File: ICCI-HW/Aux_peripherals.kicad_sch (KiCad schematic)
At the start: 35 parts

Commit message: usb PD started
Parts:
- added C? (x4): 100n, symbol Device:C
- added C? (x3): 4.7u, symbol Device:C
- added D?: Bat60B, symbol Device:D_Schottky
- added FB? (x2): BLM15HD102SN1D, symbol Device:FerriteBead_Small
- added NT?: NetTie_2, symbol Device:NetTie_2
- added R? (x3): R, symbol Device:R
- BT?: value Battery_Cell -> 2032 Cell
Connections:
- net VBATT is gone; now on net VBAT: R?.2, U?.3 (V_BCKP)
- net +3V3: now also U?.20 (VDD), C?.1, C?.1, C?.1, C?.1, R?.1, R?.1, R?.1
- net GND: now also U?.2 (MOSI), U?.8 (VSS), C?.2, C?.2, C?.2, C?.2, C?.2, C?.2, C?.2
- net RXD: now also FB?.1
- net TXD: now also FB?.1
- net SCL: now reaches U?.1 (SCL)
- net PFI: now reaches U?.14 (~{PFO})
- net ~{PFO}: now reaches U?.15 (PFI)
- net ~{PFO}: now also R?.2
- net ~{RTS}: now reaches U?.16 (~{RTS})
- net ~{RTS}: now also R?.2
- net ~{INT}: now reaches U?.17 (~{INT})
- net BBS: now reaches U?.18 (BBS)
- net BBS: now also NT?.2
- net VBAT: now reaches U?.19 (VBAT)
- net VBAT: now also C?.1, C?.1, C?.1, D?.1 (K)
- net SDA: now reaches U?.4 (SDA/~{CE})
- net IFS: now reaches U?.5 (IFS)
- net IFS: now also NT?.1
- net ~{TS}: now reaches U?.6 (~{TS})
- net CLKOUT: now reaches U?.7 (CLKOUT)
- net CLKOUT: now also R?.2
- net at BT?.1 (+): now also D?.2 (A)
- net EXTINT renamed GPS_EXTINT
- net TP renamed GPS_TP
- net ~{RESET} renamed ~{GPS_RESET}
- new net GPS_RXD: FB?.2
- new net GPS_TXD: FB?.2
- no-connect marks 2 -> 3
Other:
- note added: "BATT on GPS for hot start"
- note added: "BATT on RTC for time"
- note added: "FORK RTC/GPS GITHUB"
- note added: "VCC decoup"
- note added: "Vbat decoup"
- note removed: "Possibilità di non montarlo"
- moved on the sheet: BT?, Q?, R?, U?

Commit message: updated
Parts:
- removed C? (x4): 100n, symbol Device:C
- removed R? (x4): 10k, symbol Device:R
- removed SW?: SW_BOOT, symbol Switch:SW_Push
- removed SW?: SW_LOG_SD, symbol Switch:SW_Push
- removed SW?: SW_RST_PROV, symbol Switch:SW_Push
- removed SW?: SW_RST, symbol Switch:SW_Push
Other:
- note removed: "BUTTONS"

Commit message: updated
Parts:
- removed FB? (x2): BLM15HD102SN1D, symbol Device:FerriteBead_Small
- added R? (x2): 4.7k, symbol Device:R
- R?: Place (none) -> DNP; now left out of the parts list
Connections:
- net SCL is gone; now on net SCL1: U?.1 (SCL)
- net SDA is gone; now on net SDA1: U?.4 (SDA/~{CE})
- net +3V3: now also R?.1, R?.1
- net SCL1: now reaches U?.12 (SCL)
- net SCL1: now also R?.2
- net SDA1: now reaches U?.9 (SDA)
- net SDA1: now also R?.2
- net CLKOUT renamed RTC_CLKOUT
- net RXD: no longer names the net of U?.14 (RXD)
- net SD_CLK renamed VSPI_CLK
- net SD_MISO renamed VSPI_MISO
- net SD_MOSI renamed VSPI_MOSI
- net TXD: no longer names the net of U?.13 (TXD)
- net ~{PFO} renamed ~{RTC_PFO}
- net ~{RTS} renamed ~{RTC_RTS}
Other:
- note added: "BATT on GPS for hot start, RTC time can't be read BATT on RTC for time"
- note added: "DA CONTROLLARE TUUTA STA ROBA"
- note removed: "BATT on GPS for hot start"
- note removed: "BATT on RTC for time"
- moved on the sheet: BZ?, D?, Q?, R?

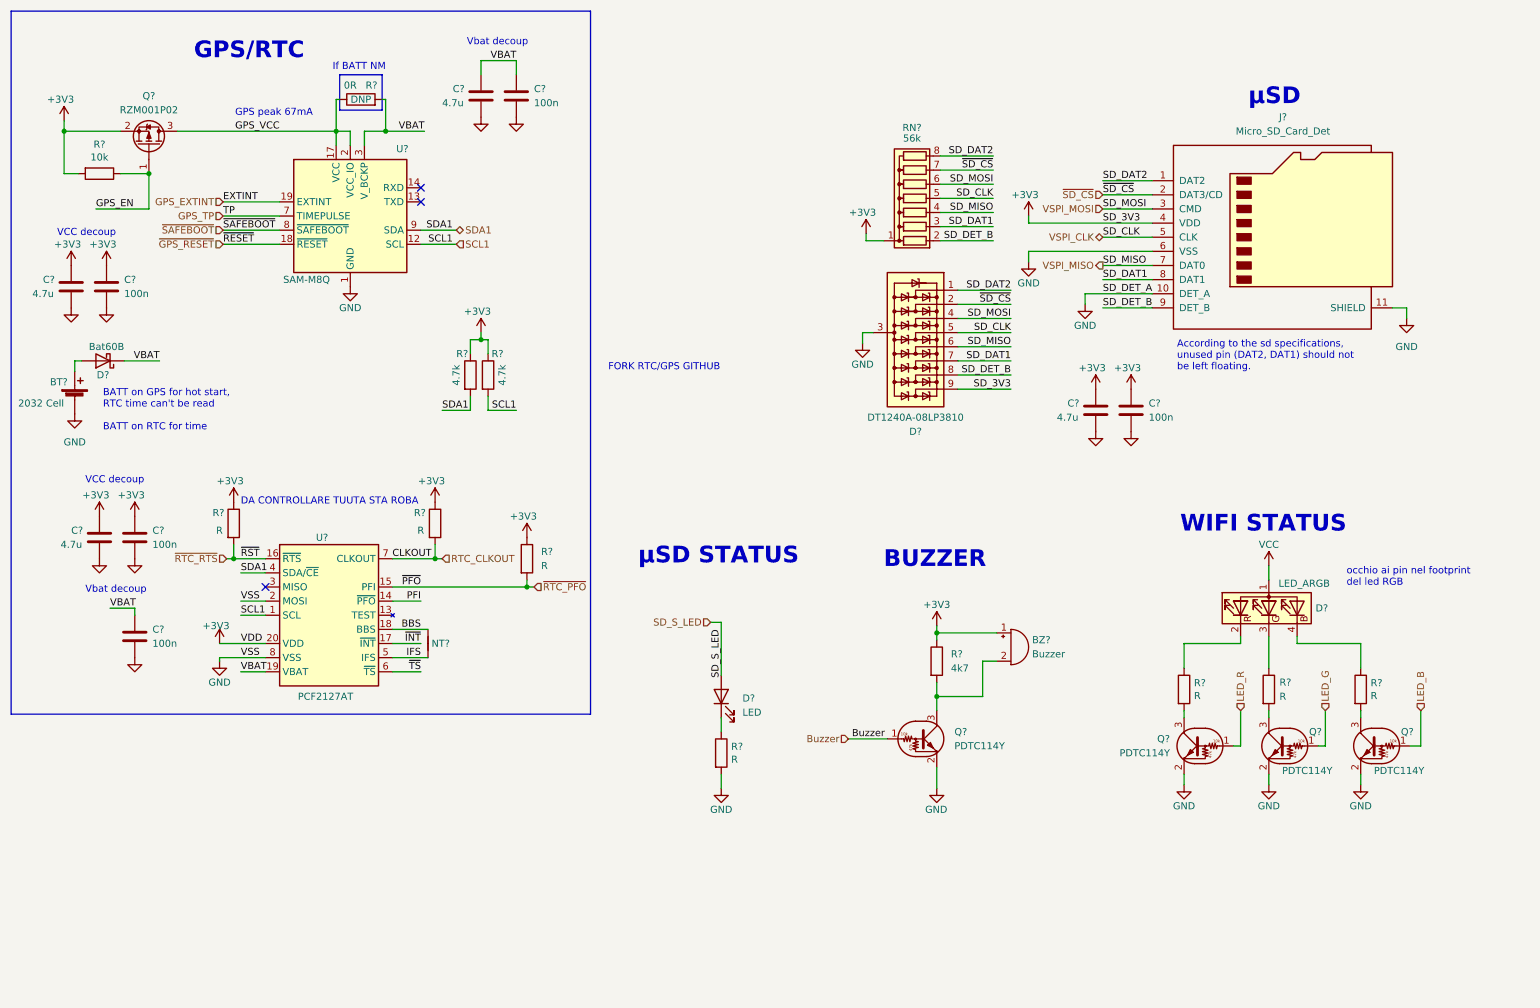
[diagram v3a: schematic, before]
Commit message: add GPIO Expansion
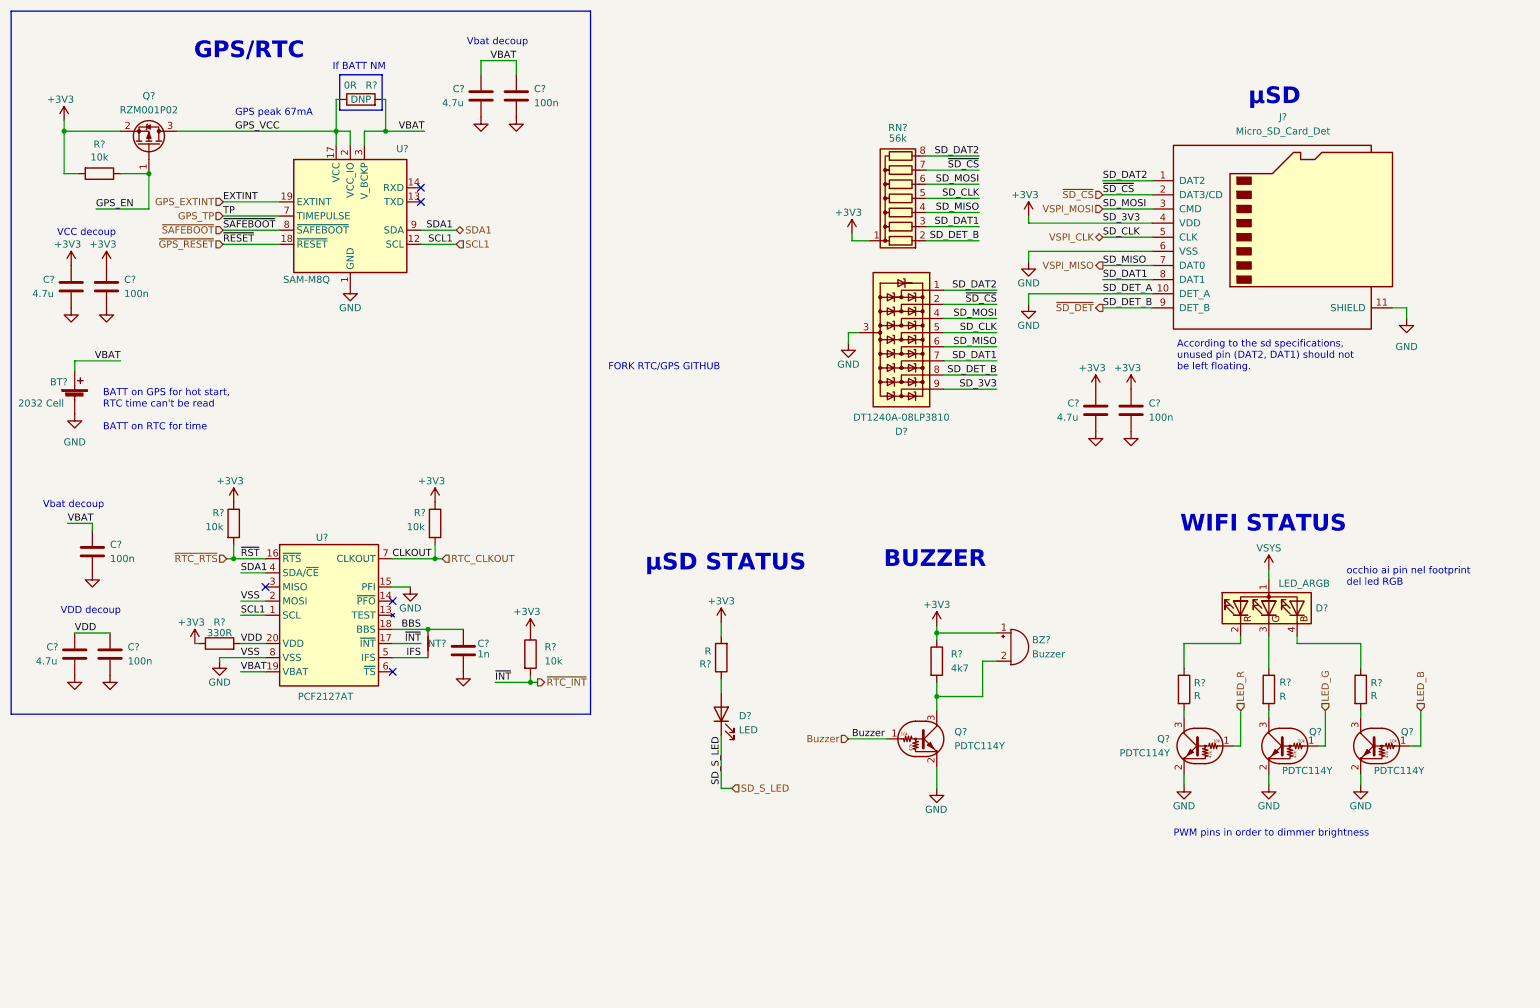
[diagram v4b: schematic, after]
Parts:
- removed D?: Bat60B, symbol Device:D_Schottky
- removed R?: R, symbol Device:R
- removed R? (x2): 4.7k, symbol Device:R
- added C?: 1n, symbol Device:C
- added R?: 330R, symbol Device:R
- added R?: 10k, symbol Device:R
- R? (x2): value R -> 10k
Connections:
- net ~{RTC_PFO} is gone; now on net GND: U?.15 (PFI)
- net +3V3: now also R?.2, R?.1, R?.1; no longer C?.1, C?.1, U?.20 (VDD)
- net BBS: now also C?.1
- net GND: now also C?.2; no longer R?.2
- net SD_S_LED: now also D?.1 (K); no longer D?.2 (A)
- net VBAT: now also BT?.1 (+)
- net at R?.1: now also D?.2 (A); no longer D?.1 (K)
- net PFI: no longer names the net of U?.14 (~{PFO})
- net SD_DET_B renamed ~{SD_DET}
- net ~{INT} renamed ~{RTC_INT}
- net ~{RTC_INT}: now also R?.2
- net ~{TS}: no longer names the net of U?.6 (~{TS})
- new net VDD: C?.1, C?.1, R?.2, U?.20 (VDD)
- no-connect marks 3 -> 5
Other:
- note added: "PWM pins in order to dimmer brightness"
- note added: "VDD decoup"
- note removed: "DA CONTROLLARE TUUTA STA ROBA"
- moved on the sheet: C?, D?, R?, RN?

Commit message: updated
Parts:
- D?: Color (none) -> Green
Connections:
- net SD_S_LED renamed ~{SD_S_LED}
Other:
- note added: "NOTE: All ESP32 output pins are PWM capable!"
- note added: "WIFI/CHARGING STATUS"
- note removed: "PWM pins in order to dimmer brightness"
- note removed: "WIFI STATUS"
- moved on the sheet: BZ?, C?, D?, J?, Q?, R?, RN?

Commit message: schematic V1.0
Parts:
- removed D?: LED_ARGB, symbol Device:LED_ARGB
- added D?: IN-P55TATRGB, symbol ICCI-LIB:IN-P55TATRGB
- added J401: EXP0, symbol Connector:Conn_01x04_Male
- added J402: EXP1, symbol Connector:Conn_01x04_Male
- R407: renamed from R?; value R -> 510R
- R409, R411: renamed from R?; value R -> 180R
- R410: renamed from R?; value R -> 220R
- gave numbers to parts that had none: 31
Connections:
- net +3V3: now also J401.1 (Pin_1), J402.1 (Pin_1)
- net GND: now also J401.4 (Pin_4), J402.4 (Pin_4)
- net SCL1: now also J402.2 (Pin_2)
- net SDA1: now also J402.3 (Pin_3)
- net at R409.1: now also D?.1
- net at R410.1: now also D?.2
- net at R411.1: now also D?.3
- net VBAT renamed 3V_BAT
- net ~{SAFEBOOT}: no longer names the net of U402.8 (~{SAFEBOOT})
- new net SCL0: J401.2 (Pin_2)
- new net SDA0: J401.3 (Pin_3)
- new net VBUS: D?.4, D?.5, D?.6
- no-connect marks 5 -> 6
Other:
- note added: "I2C Expansions"
- note removed: "NOTE: All ESP32 output pins are PWM capable!"
- note removed: "occhio ai pin nel footprint del led RGB"

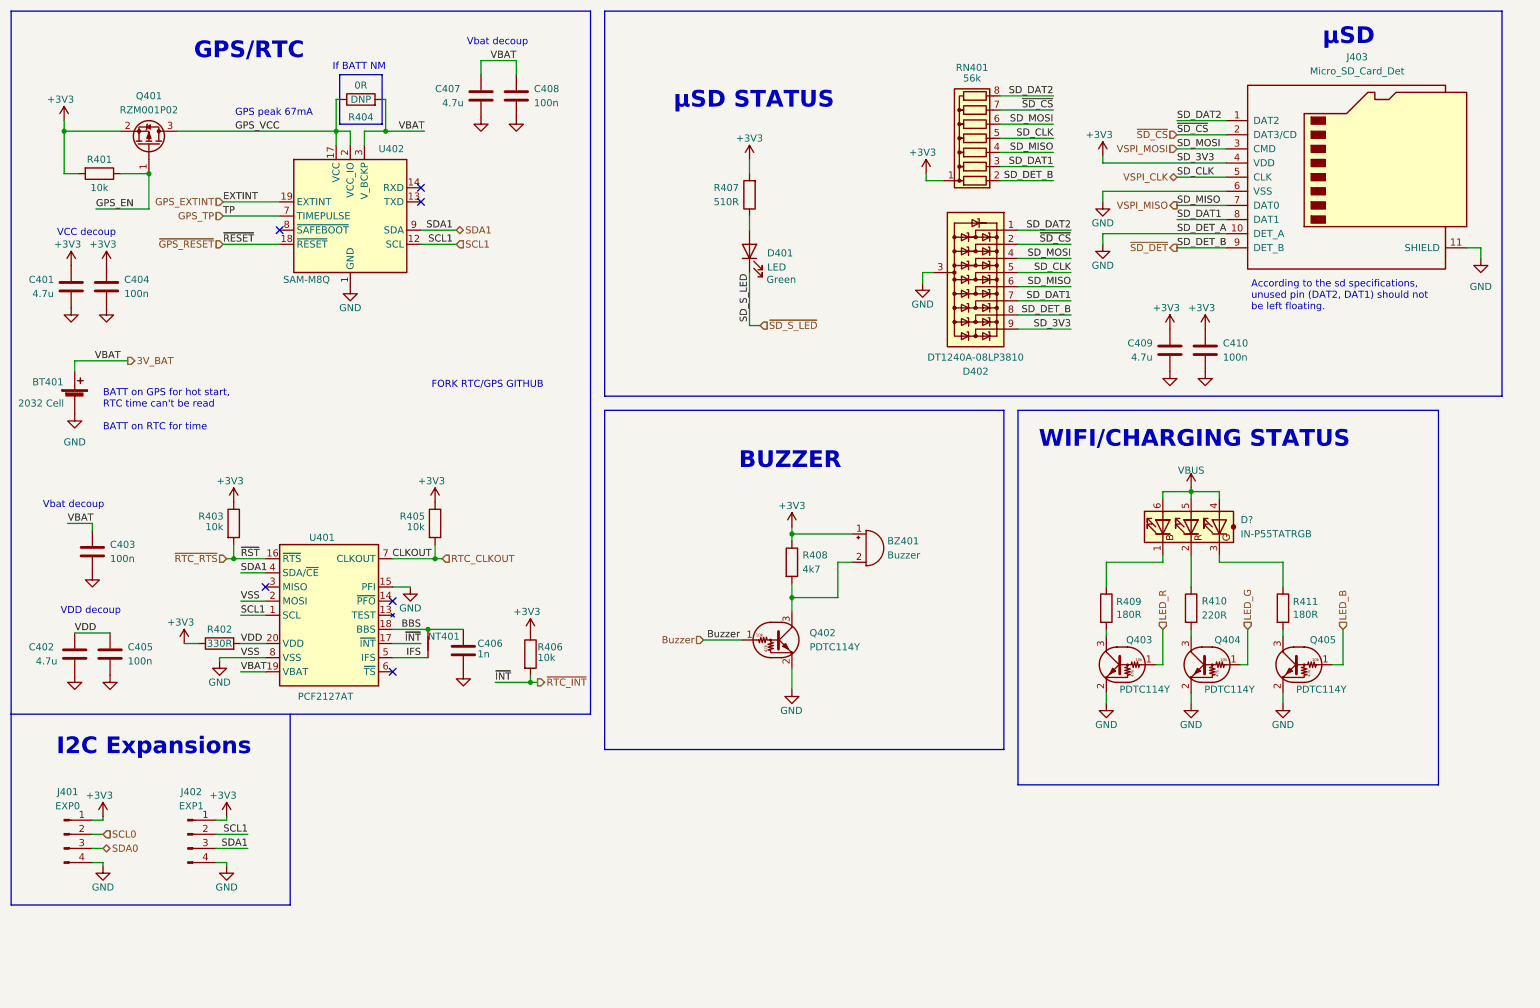
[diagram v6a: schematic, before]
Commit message: footprint assigned
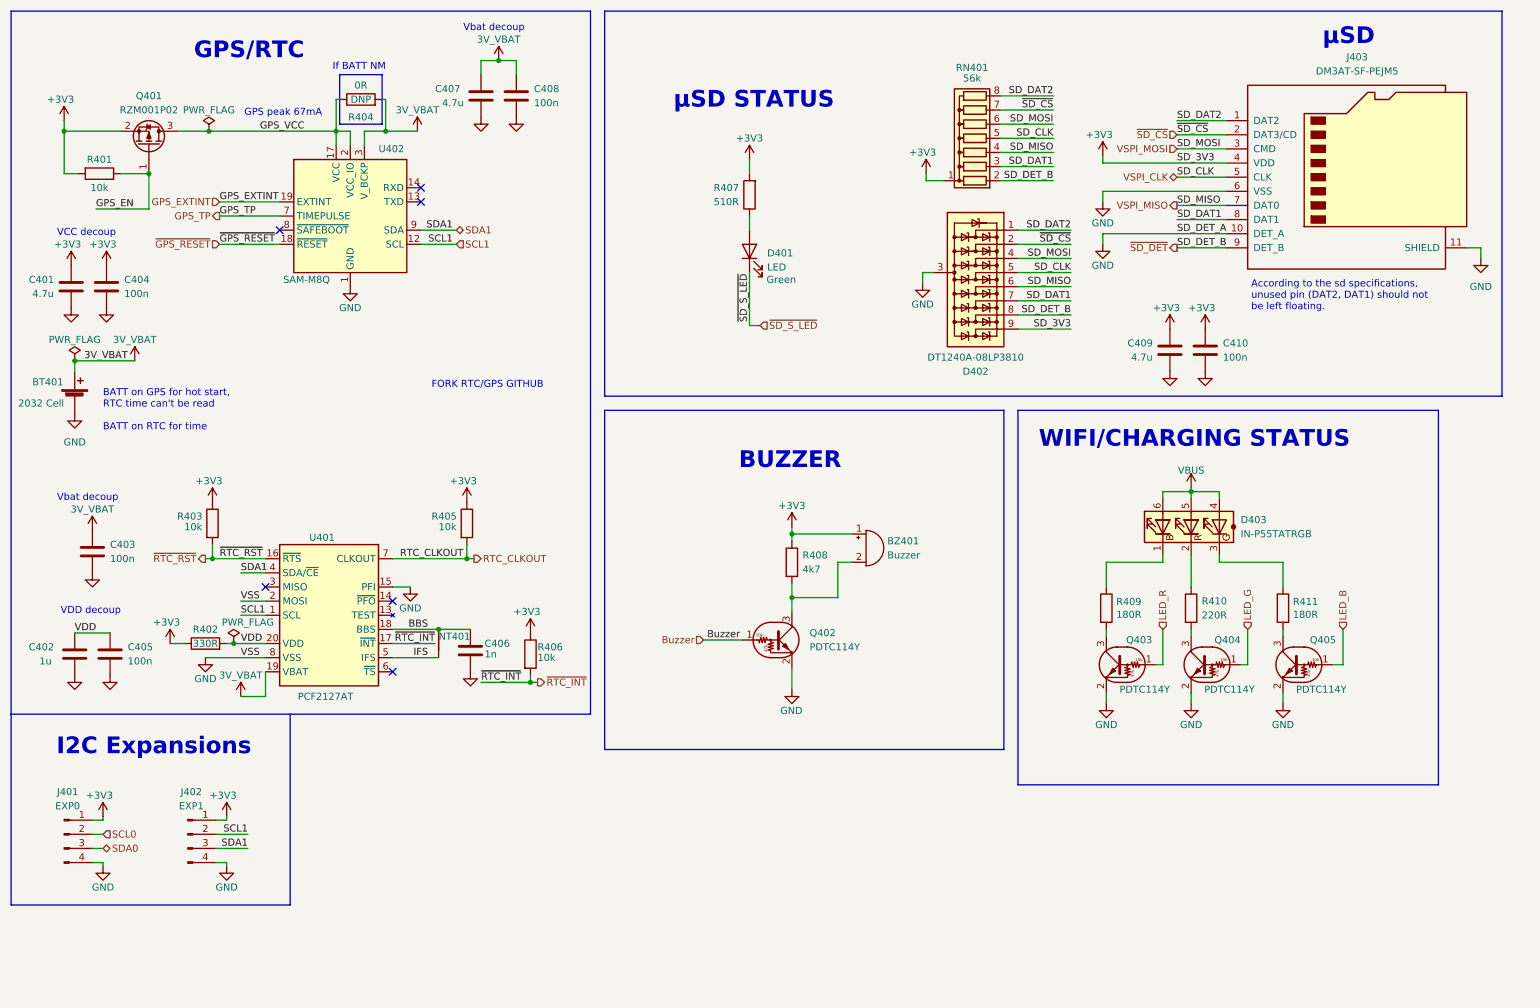
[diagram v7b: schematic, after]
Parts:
- BT401: footprint (none) -> Battery:BatteryHolder_Keystone_3034_1x20mm
- BZ401: footprint Buzzer_Beeper:Buzzer_12x9.5RM7.6 -> ICCI-LIB:PiezoBuzzer_17_P10; Model (none) -> PS1740P02E
- C401, C403, C404, C405, C406, C407, C408, C409, C410: footprint (none) -> Capacitor_SMD:C_0603_1608Metric
- C402: value 4.7u -> 1u; footprint (none) -> Capacitor_SMD:C_0603_1608Metric
- D401: footprint (none) -> LED_SMD:LED_0805_2012Metric
- D403: renamed from D?; footprint (none) -> ICCI-LIB:LED_IN-P55TATRGB
- J401, J402: footprint (none) -> Connector_PinHeader_2.54mm:PinHeader_1x04_P2.54mm_Vertical
- J403: value Micro_SD_Card_Det -> DM3AT-SF-PEJM5; footprint (none) -> Connector_Card:microSD_HC_Hirose_DM3AT-SF-PEJM5
- NT401: footprint (none) -> NetTie:NetTie-2_SMD_Pad0.5mm
- Q401: footprint (none) -> ICCI-LIB:RZM001P02
- R402: footprint (none) -> Resistor_SMD:R_0805_2012Metric
- R403, R404, R405, R406: footprint (none) -> Resistor_SMD:R_0603_1608Metric
- RN401: footprint Resistor_THT:R_Array_SIP8 -> Resistor_SMD:R_Array_Convex_8x0602
- U401: footprint (none) -> ICCI-LIB:PCF2127AT
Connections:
- net 3V_BAT renamed +3V0
- net ~{RTC_RTS} renamed ~{RTC_RST}
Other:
- moved on the sheet: C406, NT401, R402, R403, R405

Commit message: fw: updates
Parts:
- removed D403: IN-P55TATRGB, ICCI-LIB:LED_IN-P55TATRGB, symbol ICCI-LIB:IN-P55TATRGB
- removed RN401: 56k, Resistor_SMD:R_Array_Convex_8x0602, symbol Device:R_Network07
- added D403: LED RGB 5mm Horiz., ICCI-LIB:LED_D5.0mm-4_RGB_Staggered_Pins_Horizontal, symbol Device:LED_ABGR
- added RN401: 56k, Resistor_SMD:R_Array_Convex_8x0602, symbol Device:R_Pack08
- BT401: Link (none) -> https://www.mouser.it/ProductDetail/Keystone-Electronics/30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
- BZ401: value Buzzer -> PS1240P02BT; footprint ICCI-LIB:PiezoBuzzer_17_P10 -> Buzzer_Beeper:Buzzer_TDK_PS1240P02BT_D12.2mm_H6.5mm; Link (none) -> https://www.mouser.it/ProductDetail/TDK/PS1240P02BT?qs=d7g9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
- D401: value LED -> uSD_S_LED 5mm Horiz.; footprint LED_SMD:LED_0805_2012Metric -> LED_THT:LED_D5.0mm_Horizontal_O3.81mm_Z3.0mm
- NT401: now left out of the parts list
- R402: footprint Resistor_SMD:R_0805_2012Metric -> Resistor_SMD:R_0603_1608Metric
- R404: now in the parts list
- R407: value 510R -> 330R
- R408: value 4k7 -> 4.7k
- R409: value 180R -> 330R
- R411: value 180R -> 220R
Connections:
- net +3V3: now also RN401.10 (R7.2), RN401.11 (R6.2), RN401.12 (R5.2), RN401.13 (R4.2), RN401.14 (R3.2), RN401.15 (R2.2), RN401.16 (R1.2), RN401.9 (R8.2)
- net SD_DAT1: now also RN401.2 (R2.1)
- net SD_DAT2: now also RN401.7 (R7.1)
- net VSPI_CLK: now also RN401.4 (R4.1)
- net VSPI_MISO: now also RN401.3 (R3.1)
- net VSPI_MOSI: now also RN401.5 (R5.1)
- net ~{SD_CS}: now also RN401.6 (R6.1)
- net ~{SD_DET}: now also RN401.1 (R1.1)
- net at U401.13 (TEST): now also U401.10, U401.11, U401.12, U401.9
- net at R409.1: now also D403.1 (RK)
- net at R410.1: now also D403.4 (GK)
- net at R411.1: now also D403.3 (BK)
- net GPS_EN renamed ~{GPS_EN}
- new net VCC: D403.2 (A)
- no-connect marks 6 -> 7
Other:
- note added: "2032 BATT."
- note added: "6.4V min - 8.4V max"
- note added: "BATT on GPS for hot start, BATT on RTC for time"
- note added: "Vf=2.2-2.8V @20mA"
- note added: "Vf=3.3-4.0V @20mA"
- note added: "Vf=3.3-4.1V @20mA"
- note added: "You can use GPS or RTC depending on your needs. W: If you decide to use RTC do not place GPS components and vice-versa."
- note removed: "BATT on GPS for hot start, RTC time can't be read BATT on RTC for time"
- note removed: "FORK RTC/GPS GITHUB"
